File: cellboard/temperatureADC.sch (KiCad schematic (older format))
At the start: 17 parts, among them J1 Conn_02x08, Q19 TSM3401CX RFG, U6 ADC128D818

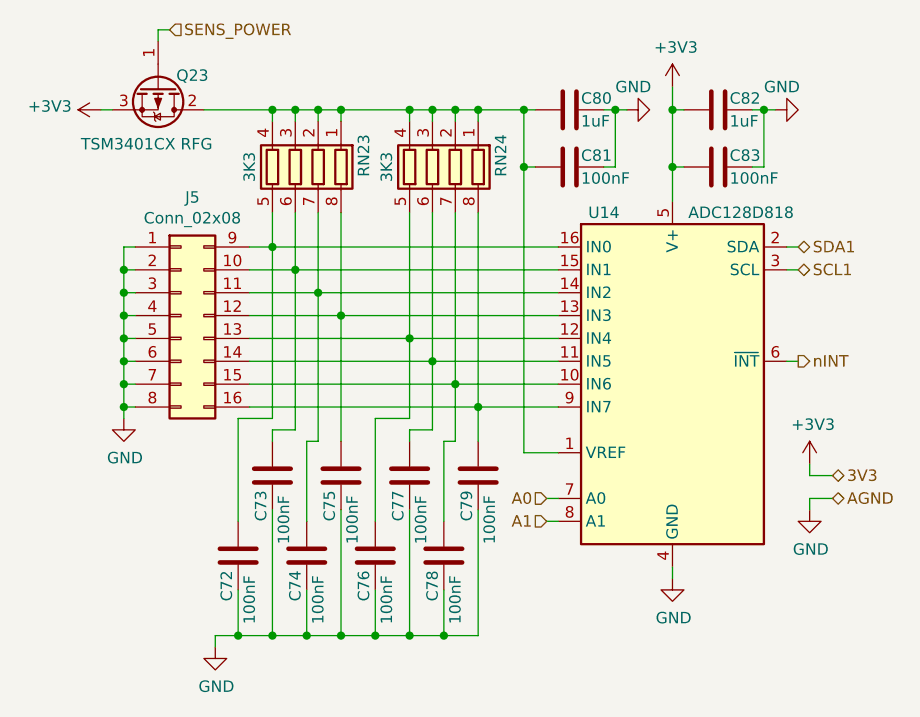
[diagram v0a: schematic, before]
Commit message: removed rescue references and rescue library
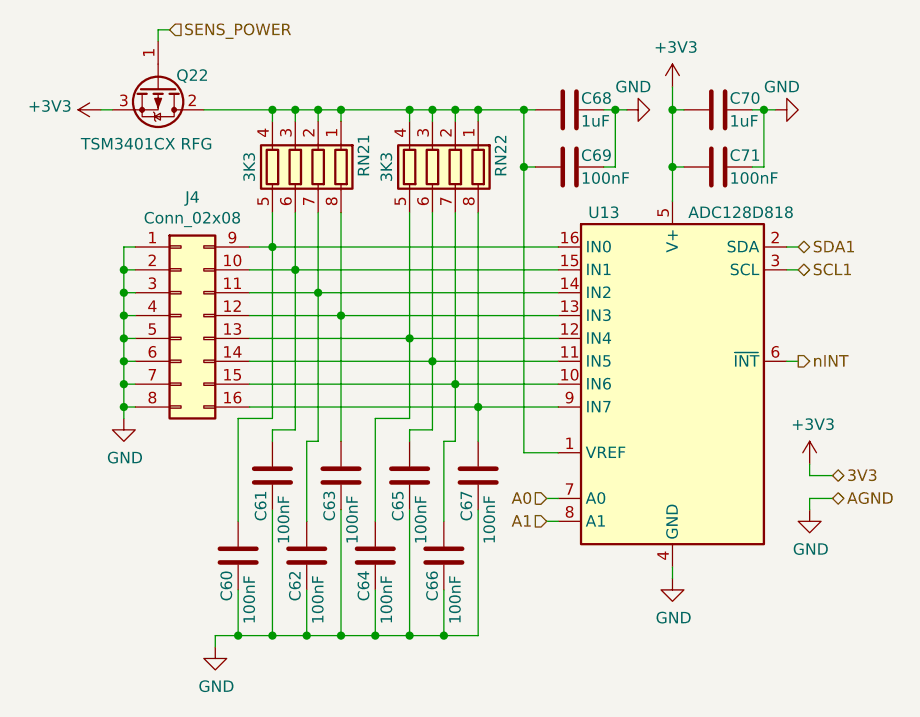
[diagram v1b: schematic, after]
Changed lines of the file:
@@
 $Descr A4 11693 8268
 encoding utf-8
-Sheet 6 10
+Sheet 8 10
 Title ""
 Date ""
@@
 AR Path="/5DECF668/5DEB8198/603EB234/604F734D" Ref="U?"  Part="1"
 AR Path="/5DECF668/5DEB8198/603F21A8/604F734D" Ref="U14"  Part="1"
-F 0 "U14" H 5200 3900 50  0000 C CNN
+F 0 "U13" H 5200 3900 50  0000 C CNN
 F 1 "ADC128D818" H 5800 3900 50  0000 C CNN
 F 2 "CellsBoard:TSSOP-16_4.4x5mm_P0.65mm" H 5500 3150 50  0001 C CIN
@@
 AR Path="/5DECF668/5DEB8198/603EB234/604FB178" Ref="#PWR?"  Part="1"
 AR Path="/5DECF668/5DEB8198/603F21A8/604FB178" Ref="#PWR064"  Part="1"
-F 0 "#PWR064" H 5500 3750 50  0001 C CNN
+F 0 "#PWR055" H 5500 3750 50  0001 C CNN
 F 1 "GND" H 5505 3827 50  0000 C CNN
 F 2 "" H 5500 4000 50  0001 C CNN
@@
 AR Path="/5DECF668/5DEB8198/603EB234/60530696" Ref="RN?"  Part="1"
 AR Path="/5DECF668/5DEB8198/603F21A8/60530696" Ref="RN23"  Part="1"
-F 0 "RN23" V 3550 2150 50  0000 C CNN
+F 0 "RN21" V 3550 2150 50  0000 C CNN
 F 1 "3K3" V 4050 2200 50  0000 C CNN
 F 2 "Resistor_SMD:R_Array_Convex_4x1206" V 4125 2200 50  0001 C CNN
@@
 AR Path="/5DECF668/5DEB8198/603EB234/605310D0" Ref="RN?"  Part="1"
 AR Path="/5DECF668/5DEB8198/603F21A8/605310D0" Ref="RN24"  Part="1"
-F 0 "RN24" V 4150 2150 50  0000 C CNN
+F 0 "RN22" V 4150 2150 50  0000 C CNN
 F 1 "3K3" V 4650 2200 50  0000 C CNN
 F 2 "Resistor_SMD:R_Array_Convex_4x1206" V 4725 2200 50  0001 C CNN
@@
 AR Path="/5DECF668/5DEB8198/603EB234/6054A4BC" Ref="C?"  Part="1"
 AR Path="/5DECF668/5DEB8198/603F21A8/6054A4BC" Ref="C77"  Part="1"
-F 0 "C77" V 4300 3350 50  0000 L CNN
+F 0 "C65" V 4300 3350 50  0000 L CNN
 F 1 "100nF" V 4400 3250 50  0000 L CNN
 F 2 "Capacitor_SMD:C_0603_1608Metric" H 4388 3400 50  0001 C CNN
@@
 AR Path="/5DECF668/5DEB8198/603EB234/605573AD" Ref="C?"  Part="1"
 AR Path="/5DECF668/5DEB8198/603F21A8/605573AD" Ref="C79"  Part="1"
-F 0 "C79" V 4600 3350 50  0000 L CNN
+F 0 "C67" V 4600 3350 50  0000 L CNN
 F 1 "100nF" V 4700 3250 50  0000 L CNN
 F 2 "Capacitor_SMD:C_0603_1608Metric" H 4688 3400 50  0001 C CNN
@@
 AR Path="/5DECF668/5DEB8198/603EB234/605584AB" Ref="C?"  Part="1"
 AR Path="/5DECF668/5DEB8198/603F21A8/605584AB" Ref="C76"  Part="1"
-F 0 "C76" V 4150 3700 50  0000 L CNN
+F 0 "C64" V 4150 3700 50  0000 L CNN
 F 1 "100nF" V 4250 3600 50  0000 L CNN
 F 2 "Capacitor_SMD:C_0603_1608Metric" H 4238 3750 50  0001 C CNN
@@
 AR Path="/5DECF668/5DEB8198/603EB234/605587FC" Ref="C?"  Part="1"
 AR Path="/5DECF668/5DEB8198/603F21A8/605587FC" Ref="C75"  Part="1"
-F 0 "C75" V 4000 3350 50  0000 L CNN
+F 0 "C63" V 4000 3350 50  0000 L CNN
 F 1 "100nF" V 4100 3250 50  0000 L CNN
 F 2 "Capacitor_SMD:C_0603_1608Metric" H 4088 3400 50  0001 C CNN
@@
 AR Path="/5DECF668/5DEB8198/603EB234/60559061" Ref="C?"  Part="1"
 AR Path="/5DECF668/5DEB8198/603F21A8/60559061" Ref="C78"  Part="1"
-F 0 "C78" V 4450 3700 50  0000 L CNN
+F 0 "C66" V 4450 3700 50  0000 L CNN
 F 1 "100nF" V 4550 3600 50  0000 L CNN
 F 2 "Capacitor_SMD:C_0603_1608Metric" H 4538 3750 50  0001 C CNN
@@
 AR Path="/5DECF668/5DEB8198/603EB234/6056673B" Ref="C?"  Part="1"
 AR Path="/5DECF668/5DEB8198/603F21A8/6056673B" Ref="C72"  Part="1"
-F 0 "C72" V 3550 3700 50  0000 L CNN
+F 0 "C60" V 3550 3700 50  0000 L CNN
 F 1 "100nF" V 3650 3600 50  0000 L CNN
 F 2 "Capacitor_SMD:C_0603_1608Metric" H 3638 3750 50  0001 C CNN
@@
 AR Path="/5DECF668/5DEB8198/603EB234/60566AAA" Ref="C?"  Part="1"
 AR Path="/5DECF668/5DEB8198/603F21A8/60566AAA" Ref="C74"  Part="1"
-F 0 "C74" V 3850 3700 50  0000 L CNN
+F 0 "C62" V 3850 3700 50  0000 L CNN
 F 1 "100nF" V 3950 3600 50  0000 L CNN
 F 2 "Capacitor_SMD:C_0603_1608Metric" H 3938 3750 50  0001 C CNN
@@
 AR Path="/5DECF668/5DEB8198/603EB234/605671D5" Ref="C?"  Part="1"
 AR Path="/5DECF668/5DEB8198/603F21A8/605671D5" Ref="C73"  Part="1"
-F 0 "C73" V 3700 3350 50  0000 L CNN
+F 0 "C61" V 3700 3350 50  0000 L CNN
 F 1 "100nF" V 3800 3250 50  0000 L CNN
 F 2 "Capacitor_SMD:C_0603_1608Metric" H 3788 3400 50  0001 C CNN
@@
 AR Path="/5DECF668/5DEB8198/603EB234/6059FDFF" Ref="#PWR?"  Part="1"
 AR Path="/5DECF668/5DEB8198/603F21A8/6059FDFF" Ref="#PWR061"  Part="1"
-F 0 "#PWR061" H 3500 4050 50  0001 C CNN
+F 0 "#PWR052" H 3500 4050 50  0001 C CNN
 F 1 "GND" H 3505 4127 50  0000 C CNN
 F 2 "" H 3500 4300 50  0001 C CNN
@@
 AR Path="/5DECF668/5DEB8198/603EB234/605C003B" Ref="#PWR?"  Part="1"
 AR Path="/5DECF668/5DEB8198/603F21A8/605C003B" Ref="#PWR060"  Part="1"
-F 0 "#PWR060" H 3100 3050 50  0001 C CNN
+F 0 "#PWR051" H 3100 3050 50  0001 C CNN
 F 1 "GND" H 3105 3127 50  0000 C CNN
 F 2 "" H 3100 3300 50  0001 C CNN
@@
 AR Path="/5DECF668/5DEB8198/603EB234/605CF54A" Ref="C?"  Part="1"
 AR Path="/5DECF668/5DEB8198/603F21A8/605CF54A" Ref="C81"  Part="1"
-F 0 "C81" V 5000 2250 50  0000 L CNN
+F 0 "C69" V 5000 2250 50  0000 L CNN
 F 1 "100nF" V 5100 2250 50  0000 L CNN
 F 2 "Capacitor_SMD:C_0603_1608Metric" H 5088 2050 50  0001 C CNN
@@
 AR Path="/5DECF668/5DEB8198/603EB234/605D8DEB" Ref="#PWR?"  Part="1"
 AR Path="/5DECF668/5DEB8198/603F21A8/605D8DEB" Ref="#PWR065"  Part="1"
-F 0 "#PWR065" H 5950 1700 50  0001 C CNN
+F 0 "#PWR056" H 5950 1700 50  0001 C CNN
 F 1 "GND" V 6050 2000 50  0000 R CNN
 F 2 "" H 5950 1950 50  0001 C CNN
@@
 AR Path="/5DECF668/5DEB8198/603EB234/602999FE" Ref="#PWR?"  Part="1"
 AR Path="/5DECF668/5DEB8198/603F21A8/602999FE" Ref="#PWR063"  Part="1"
-F 0 "#PWR063" H 5500 1700 50  0001 C CNN
+F 0 "#PWR054" H 5500 1700 50  0001 C CNN
 F 1 "+3V3" H 5515 2023 50  0000 C CNN
 F 2 "" H 5500 1850 50  0001 C CNN
@@
 AR Path="/5DECF668/5DEB8198/603EB234/6029A8D9" Ref="#PWR?"  Part="1"
 AR Path="/5DECF668/5DEB8198/603F21A8/6029A8D9" Ref="#PWR066"  Part="1"
-F 0 "#PWR066" H 6100 3350 50  0001 C CNN
+F 0 "#PWR057" H 6100 3350 50  0001 C CNN
 F 1 "+3V3" H 6115 3673 50  0000 C CNN
 F 2 "" H 6100 3500 50  0001 C CNN
@@
 AR Path="/5DECF668/5DEB8198/603EB234/6029BC04" Ref="#PWR?"  Part="1"
 AR Path="/5DECF668/5DEB8198/603F21A8/6029BC04" Ref="#PWR059"  Part="1"
-F 0 "#PWR059" H 3000 1800 50  0001 C CNN
+F 0 "#PWR050" H 3000 1800 50  0001 C CNN
 F 1 "+3V3" V 3015 2078 50  0000 L CNN
 F 2 "" H 3000 1950 50  0001 C CNN
@@
 AR Path="/5DECF668/5DEB8198/603EB234/602AA1CB" Ref="#PWR?"  Part="1"
 AR Path="/5DECF668/5DEB8198/603F21A8/602AA1CB" Ref="#PWR067"  Part="1"
-F 0 "#PWR067" H 6100 3450 50  0001 C CNN
+F 0 "#PWR058" H 6100 3450 50  0001 C CNN
 F 1 "GND" H 6105 3527 50  0000 C CNN
 F 2 "" H 6100 3700 50  0001 C CNN
@@
 AR Path="/5DECF668/5DEB8198/603EB234/60308D34" Ref="Q?"  Part="1"
 AR Path="/5DECF668/5DEB8198/603F21A8/60308D34" Ref="Q23"  Part="1"
-F 0 "Q23" V 3200 2000 50  0000 C CNN
+F 0 "Q22" V 3200 2000 50  0000 C CNN
 F 1 "TSM3401CX RFG" V 3500 1800 50  0000 C CNN
 F 2 "CellsBoard:SOT-23" H 3450 1950 50  0001 C CNN
@@
 AR Path="/5DECF668/5DEB8198/603EB234/605CD7AA" Ref="C?"  Part="1"
 AR Path="/5DECF668/5DEB8198/603F21A8/605CD7AA" Ref="C80"  Part="1"
-F 0 "C80" V 5000 2000 50  0000 L CNN
+F 0 "C68" V 5000 2000 50  0000 L CNN
 F 1 "1uF" V 5100 2000 50  0000 L CNN
 F 2 "Capacitor_SMD:C_0603_1608Metric" H 5088 1800 50  0001 C CNN
@@
 AR Path="/5DECF668/5DEB8198/603EB234/6033FEB4" Ref="C?"  Part="1"
 AR Path="/5DECF668/5DEB8198/603F21A8/6033FEB4" Ref="C83"  Part="1"
-F 0 "C83" V 5650 2250 50  0000 L CNN
+F 0 "C71" V 5650 2250 50  0000 L CNN
 F 1 "100nF" V 5750 2250 50  0000 L CNN
 F 2 "Capacitor_SMD:C_0603_1608Metric" H 5738 2050 50  0001 C CNN
@@
 AR Path="/5DECF668/5DEB8198/603EB234/603403C8" Ref="C?"  Part="1"
 AR Path="/5DECF668/5DEB8198/603F21A8/603403C8" Ref="C82"  Part="1"
-F 0 "C82" V 5650 2000 50  0000 L CNN
+F 0 "C70" V 5650 2000 50  0000 L CNN
 F 1 "1uF" V 5750 2000 50  0000 L CNN
 F 2 "Capacitor_SMD:C_0603_1608Metric" H 5738 1800 50  0001 C CNN
@@
 AR Path="/5DECF668/5DEB8198/603EB234/60354C60" Ref="#PWR?"  Part="1"
 AR Path="/5DECF668/5DEB8198/603F21A8/60354C60" Ref="#PWR062"  Part="1"
-F 0 "#PWR062" H 5300 1700 50  0001 C CNN
+F 0 "#PWR053" H 5300 1700 50  0001 C CNN
 F 1 "GND" V 5400 2000 50  0000 R CNN
 F 2 "" H 5300 1950 50  0001 C CNN
@@
 AR Path="/5DECF668/5DEB8198/603F21A8/604F6B66" Ref="J5"  Part="1"
 AR Path="/604F6B66" Ref="J1"  Part="1"
-F 0 "J5" H 3400 3367 50  0000 C CNN
+F 0 "J4" H 3400 3367 50  0000 C CNN
 F 1 "Conn_02x08" H 3400 3276 50  0000 C CNN
 F 2 "CellsBoard:Molex_Micro-Fit_3.0_43045-1612_2x08_P3.00mm_Vertical" H 3350 2850 50  0001 C CNN
